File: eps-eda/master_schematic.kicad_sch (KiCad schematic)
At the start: 2 parts

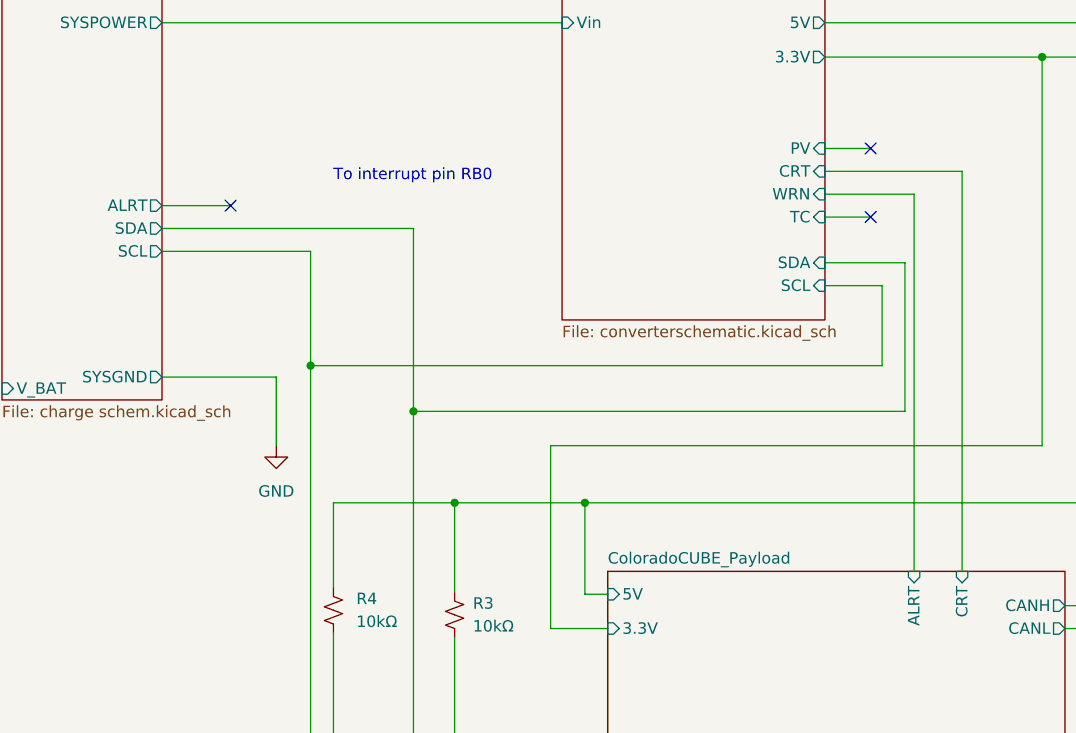
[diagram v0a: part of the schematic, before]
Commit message: rev 0.2 update
added 90deg pic adapter to include an edge cutout.

changed footprint of fuel gauge to implement ALRT signal.

rotated battery connector to better implement with the battery board.

Co-Authored-By: ajbrannigan <91212154+ajbrannigan@users.noreply.github.com>
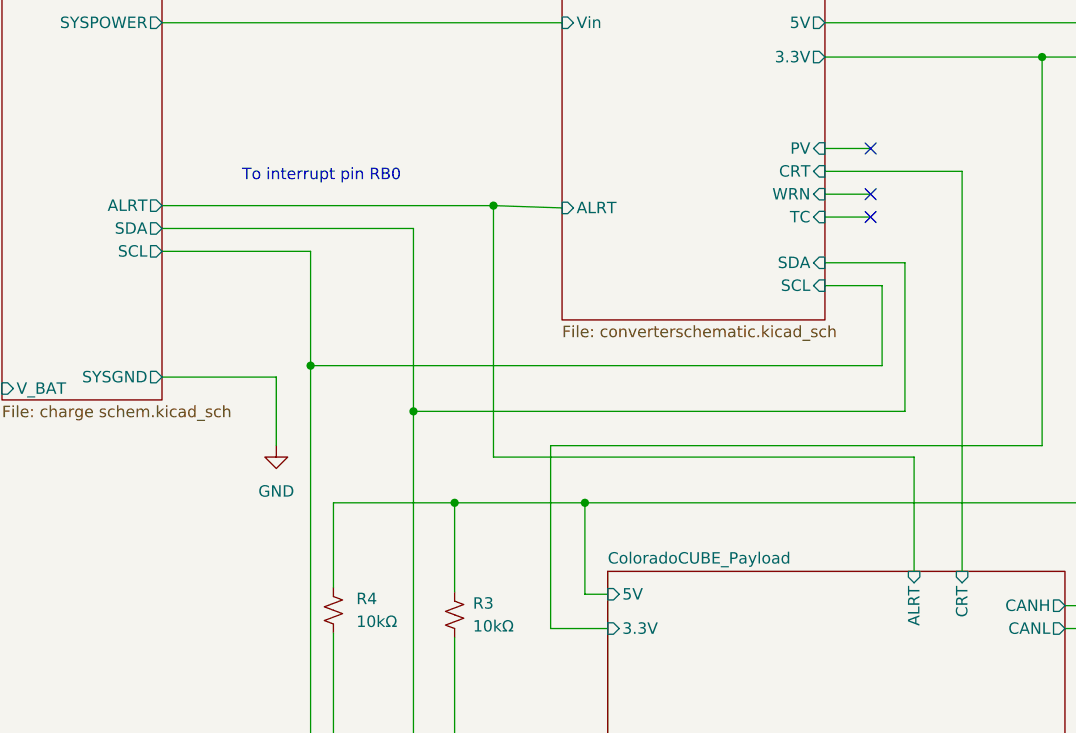
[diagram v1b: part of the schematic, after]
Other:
- sheet converterschematic ports: added ALRT; removed none
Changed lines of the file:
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@@
   (junction (at 93.98 105.41) (diameter 0) (color 0 0 0 0)
   )
+  (junction (at 114.3 87.63) (diameter 0) (color 0 0 0 0)
+  )
   (junction (at 96.52 151.13) (diameter 0) (color 0 0 0 0)
   )
@@
   (junction (at 198.12 67.31) (diameter 0) (color 0 0 0 0)
   )
-  (no_connect (at 85.09 87.63))
   (no_connect (at 156.21 81.28))
   (no_connect (at 156.21 88.9))
+  (no_connect (at 156.21 86.36))
   (no_connect (at 237.49 80.01))
   (no_connect (at 237.49 69.85))
@@
     (stroke (width 0) (type default) (color 0 0 0 0))
   )
+  (wire (pts (xy 114.3 87.63) (xy 114.3 115.57))
+    (stroke (width 0) (type default) (color 0 0 0 0))
+  )
   (wire (pts (xy 198.12 73.66) (xy 198.12 71.12))
     (stroke (width 0) (type default) (color 0 0 0 0))
@@
     (stroke (width 0) (type default) (color 0 0 0 0))
   )
+  (wire (pts (xy 161.036 115.57) (xy 161.036 128.27))
+    (stroke (width 0) (type default) (color 0 0 0 0))
+  )
   (wire (pts (xy 96.52 151.13) (xy 127 151.13))
     (stroke (width 0) (type default) (color 0 0 0 0))
@@
     (stroke (width 0) (type default) (color 0 0 0 0))
   )
+  (wire (pts (xy 77.47 87.63) (xy 114.3 87.63))
+    (stroke (width 0) (type default) (color 0 0 0 0))
+  )
   (wire (pts (xy 120.65 134.62) (xy 120.65 114.3))
     (stroke (width 0) (type default) (color 0 0 0 0))
@@
     (stroke (width 0) (type default) (color 0 0 0 0))
   )
-  (wire (pts (xy 77.47 87.63) (xy 85.09 87.63))
-    (stroke (width 0) (type default) (color 0 0 0 0))
-  )
   (wire (pts (xy 105.41 110.49) (xy 105.41 147.32))
     (stroke (width 0) (type default) (color 0 0 0 0))
@@
     (stroke (width 0) (type default) (color 0 0 0 0))
   )
+  (wire (pts (xy 151.13 86.36) (xy 156.21 86.36))
+    (stroke (width 0) (type default) (color 0 0 0 0))
+  )
   (wire (pts (xy 151.13 93.98) (xy 160.02 93.98))
     (stroke (width 0) (type default) (color 0 0 0 0))
   )
+  (wire (pts (xy 114.3 115.57) (xy 161.036 115.57))
+    (stroke (width 0) (type default) (color 0 0 0 0))
+  )
+  (wire (pts (xy 121.92 87.884) (xy 114.3 87.63))
+    (stroke (width 0) (type default) (color 0 0 0 0))
+  )
   (wire (pts (xy 177.8 134.62) (xy 201.93 134.62))
     (stroke (width 0) (type default) (color 0 0 0 0))
@@
     (stroke (width 0) (type default) (color 0 0 0 0))
   )
-  (wire (pts (xy 151.13 86.36) (xy 161.036 86.36))
-    (stroke (width 0) (type default) (color 0 0 0 0))
-  )
   (wire (pts (xy 186.69 120.65) (xy 186.69 67.31))
     (stroke (width 0) (type default) (color 0 0 0 0))
@@
   )
   (wire (pts (xy 93.98 151.13) (xy 96.52 151.13))
-    (stroke (width 0) (type default) (color 0 0 0 0))
-  )
-  (wire (pts (xy 161.036 86.36) (xy 161.036 128.27))
     (stroke (width 0) (type default) (color 0 0 0 0))
   )
@@
     (effects (font (size 1.27 1.27)) (justify left bottom))
   )
-  (text "To interrupt pin RB0" (at 96.52 85.09 0)
+  (text "To interrupt pin RB0" (at 86.36 85.09 0)
     (effects (font (size 1.27 1.27)) (justify left bottom))
   )
@@
       (effects (font (size 1.27 1.27)) (justify left))
     )
+    (pin "ALRT" input (at 121.92 87.884 180)
+      (effects (font (size 1.27 1.27)) (justify left))
+    )
   )
   (sheet_instances
@@
     (path "/59a4dc33-016c-4cea-b648-6fe1c8836f68" (page "2"))
     (path "/26a06af6-a463-4c0b-bc99-b7ef2964e4cd" (page "3"))
+    (path "/3a06e4e0-634b-426a-a0ab-d37016f35ddc/4e16fedc-a38b-401e-a5de-03896de0e471" (page "#"))
     (path "/009ce997-1584-43ca-93af-c5bcacd4d4e9" (page "5"))
     (path "/3a06e4e0-634b-426a-a0ab-d37016f35ddc" (page "6"))
-    (path "/3a06e4e0-634b-426a-a0ab-d37016f35ddc/4e16fedc-a38b-401e-a5de-03896de0e471" (page "#"))
     (path "/3a06e4e0-634b-426a-a0ab-d37016f35ddc/a47b42ae-0735-4637-85df-404ec278273a" (page "#"))
   )
@@
     )
     (path "/3a06e4e0-634b-426a-a0ab-d37016f35ddc/4e16fedc-a38b-401e-a5de-03896de0e471/3cb6757c-1471-462d-bab4-7285dc5b234b"
-      (reference "J4") (unit 1) (value "Conn_01x05_Female") (footprint "Connector_PinSocket_2.54mm:PinSocket_1x05_P2.54mm_Vertical")
+      (reference "J4") (unit 1) (value "Conn_01x05_90deg") (footprint "Connector_PinHeader_2.54mm:PinHeader_1x05_P2.54mm_Horizontal")
     )
     (path "/3a06e4e0-634b-426a-a0ab-d37016f35ddc/faeec20a-7598-48a1-895a-5d19427fab50"
@@
     )
     (path "/26a06af6-a463-4c0b-bc99-b7ef2964e4cd/62903ce9-1929-4ae0-8378-6aa7c4209eef"
-      (reference "U6") (unit 1) (value "MAX17055EWL+T") (footprint "max17055:MAX17055EWL_plus_T")
+      (reference "U6") (unit 1) (value "MAX17055ETB+T") (footprint "max17055 smd:MAX17055ETB&plus_T")
     )
     (path "/3a06e4e0-634b-426a-a0ab-d37016f35ddc/a47b42ae-0735-4637-85df-404ec278273a/ee7f89b1-017a-4a74-a6b7-58e6b5d8a56d"
